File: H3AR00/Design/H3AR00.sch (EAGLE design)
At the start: 8 parts, among them P1 HEXABIT_18.00_REVERSED, U1 TPS76433DBVT

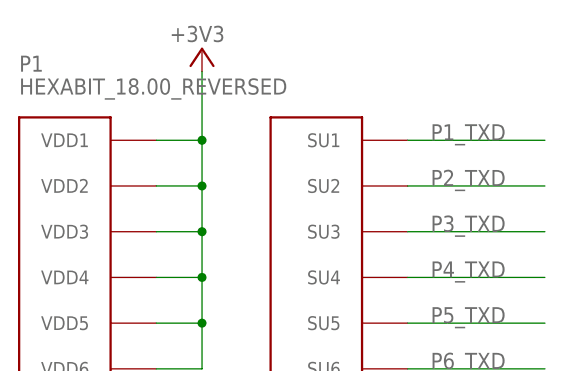
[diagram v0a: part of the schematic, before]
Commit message: Reduce module opening from side 18mm to side 17.6mm Revision 1
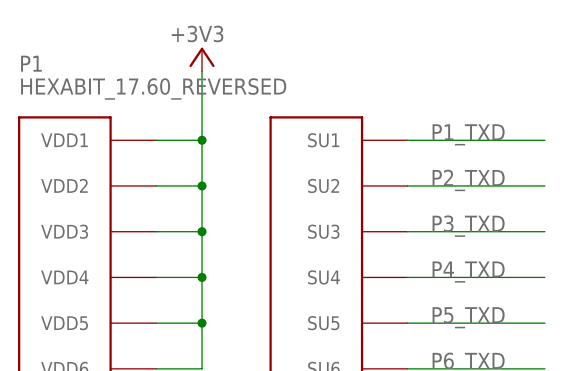
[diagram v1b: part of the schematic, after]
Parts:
- P1: value HEXABIT_18.00_REVERSED -> HEXABIT_17.60_REVERSED; device hexabitz_connectors:HEXABIT_18.00_REVERSED -> hexabitz_connectors:HEXABIT_17.60_REVERSED
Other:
- note added: "H3AR0"
- note removed: "0"
- note removed: "H3AR00"
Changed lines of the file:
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@@
 <?xml version="1.0" encoding="utf-8"?>
 <!DOCTYPE eagle SYSTEM "eagle.dtd">
-<eagle version="9.3.0">
+<eagle version="9.6.1">
 <drawing>
 <settings>
@@
 </classes>
 <parts>
-<part name="P1" library="hexabitz_connectors" deviceset="HEXABIT_?_REVERSED" device="18.00"/>
+<part name="P1" library="hexabitz_connectors" library_urn="urn:adsk.eagle:library:20064578" deviceset="HEXABIT_?_REVERSED" device="17.60" package3d_urn="urn:adsk.eagle:package:20064623/4"/>
 <part name="SUPPLY1" library="supply2" library_urn="urn:adsk.eagle:library:372" deviceset="GND" device=""/>
 <part name="P2" library="Hexabitz" deviceset="MA10-1" device="" package3d_urn="urn:adsk.eagle:package:8346/1">
@@
 <text x="215.9" y="5.3848" size="1.9304" layer="100" font="vector">Sheet   of</text>
 <text x="199.4662" y="19.6342" size="1.9304" layer="100" font="vector">Title</text>
-<text x="180.9242" y="19.6342" size="1.9304" layer="102" font="vector">H3AR00</text>
+<text x="180.9242" y="19.6342" size="1.9304" layer="102" font="vector">H3AR0</text>
 <text x="191.9478" y="11.2014" size="1.9304" layer="101" font="vector" align="center">30mm Module DIP Adapter</text>
 <text x="206.3242" y="19.6342" size="1.9304" layer="101" font="vector">H3AR00_Frontend</text>
@@
 <wire x1="168.91" y1="18.288" x2="168.91" y2="22.86" width="0.1524" layer="205"/>
 <text x="222.25" y="10.2108" size="1.9304" layer="101" font="vector">Letter</text>
-<text x="227.6602" y="14.7066" size="1.9304" layer="101" font="vector">0</text>
+<text x="227.6602" y="14.7066" size="1.9304" layer="101" font="vector">1</text>
 <text x="223.52" y="5.3848" size="1.9304" layer="101" font="vector">1</text>
 <text x="228.346" y="5.3848" size="1.9304" layer="101" font="vector">1</text>
